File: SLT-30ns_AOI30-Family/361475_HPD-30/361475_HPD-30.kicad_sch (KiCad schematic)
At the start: 7 parts, among them T1 ABC, T2 ABC, U1 12-Pin_SLx_Can

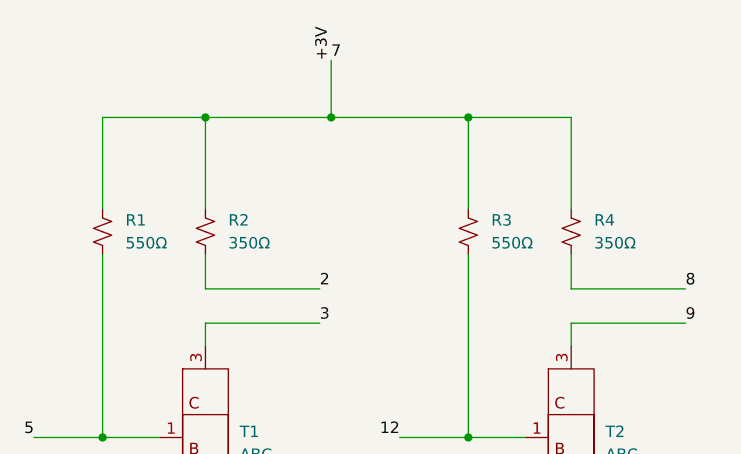
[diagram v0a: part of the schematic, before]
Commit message: Update schematic pdfs
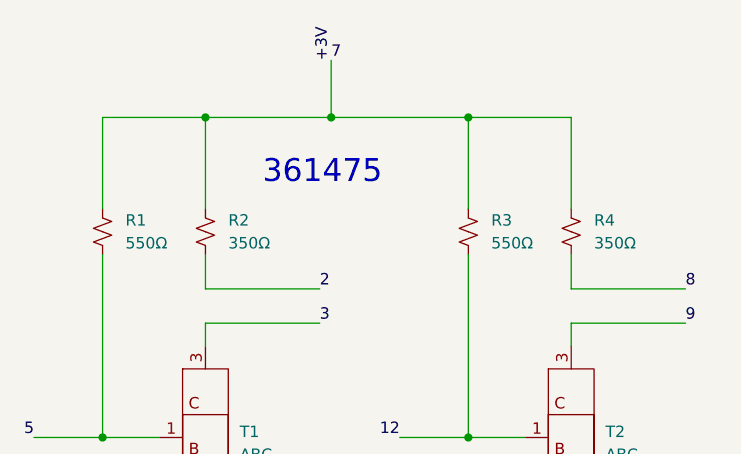
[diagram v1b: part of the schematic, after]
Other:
- note added: "361475"
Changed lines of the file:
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@@
     (stroke (width 0) (type default) (color 0 0 0 0))
+  )
+  (text "361475" (at 107.95 76.2 0)
+    (effects (font (size 2.54 2.54)) (justify left bottom))
   )
   (label "8" (at 154.94 87.63 0)
